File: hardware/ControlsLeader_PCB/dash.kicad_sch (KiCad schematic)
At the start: 11 parts, among them J11 EStop1, J12 EStop2, J13 Supp_In, J14 EStop3, J9 Supp_In

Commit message: Schematic RevA
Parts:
- J11, J12, J13, J14, J9: now fitted
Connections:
- net NMOS Switch/3.3V_LDO renamed NMOS Switch/3.3V_LDO_Switch
- net NMOS Switch1/3.3V_LDO renamed NMOS Switch1/3.3V_LDO_Switch
- net NMOS Switch2/3.3V_LDO renamed NMOS Switch2/3.3V_LDO_Switch
- net NMOS Switch3/3.3V_LDO renamed NMOS Switch3/3.3V_LDO_Switch
- net NMOS Switch4/3.3V_LDO renamed NMOS Switch4/3.3V_LDO_Switch
- net NMOS Switch5/3.3V_LDO renamed NMOS Switch5/3.3V_LDO_Switch
- net NMOS Switch6/3.3V_LDO renamed NMOS Switch6/3.3V_LDO_Switch
- net NMOS Switch8/3.3V_LDO renamed NMOS Switch8/3.3V_LDO_Switch
- net NMOS Switch9/3.3V_LDO renamed NMOS Switch9/3.3V_LDO_Switch
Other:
- sheet NMOS Switch ports: added 3.3V_LDO_Switch; removed 3.3V_LDO
- sheet NMOS Switch1 ports: added 3.3V_LDO_Switch; removed 3.3V_LDO
- sheet NMOS Switch2 ports: added 3.3V_LDO_Switch; removed 3.3V_LDO
- sheet NMOS Switch3 ports: added 3.3V_LDO_Switch; removed 3.3V_LDO
- sheet NMOS Switch4 ports: added 3.3V_LDO_Switch; removed 3.3V_LDO
- sheet NMOS Switch5 ports: added 3.3V_LDO_Switch; removed 3.3V_LDO
- sheet NMOS Switch6 ports: added 3.3V_LDO_Switch; removed 3.3V_LDO
- sheet NMOS Switch8 ports: added 3.3V_LDO_Switch; removed 3.3V_LDO
- sheet NMOS Switch9 ports: added 3.3V_LDO_Switch; removed 3.3V_LDO
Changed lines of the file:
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@@
 	(wire
 		(pts
-			(xy 218.44 54.61) (xy 219.71 54.61)
+			(xy 218.44 50.8) (xy 219.71 50.8)
 		)
 		(stroke
@@
 	(wire
 		(pts
-			(xy 218.44 90.17) (xy 219.71 90.17)
+			(xy 218.44 86.36) (xy 219.71 86.36)
 		)
 		(stroke
@@
 	(wire
 		(pts
-			(xy 120.65 107.95) (xy 121.92 107.95)
+			(xy 120.65 104.14) (xy 121.92 104.14)
 		)
 		(stroke
@@
 	(wire
 		(pts
-			(xy 123.19 86.36) (xy 124.46 86.36)
+			(xy 123.19 82.55) (xy 124.46 82.55)
 		)
 		(stroke
@@
 	(wire
 		(pts
-			(xy 120.65 125.73) (xy 121.92 125.73)
+			(xy 119.38 121.92) (xy 120.65 121.92)
 		)
 		(stroke
@@
 	(wire
 		(pts
-			(xy 123.19 52.07) (xy 124.46 52.07)
+			(xy 123.19 48.26) (xy 124.46 48.26)
 		)
 		(stroke
@@
 	(wire
 		(pts
-			(xy 120.65 142.24) (xy 121.92 142.24)
+			(xy 120.65 138.43) (xy 121.92 138.43)
 		)
 		(stroke
@@
 	(wire
 		(pts
-			(xy 218.44 107.95) (xy 219.71 107.95)
+			(xy 218.44 104.14) (xy 219.71 104.14)
 		)
 		(stroke
@@
 	(wire
 		(pts
-			(xy 123.19 69.85) (xy 124.46 69.85)
+			(xy 123.19 66.04) (xy 124.46 66.04)
 		)
 		(stroke
@@
 	(hierarchical_label "Hazard_GPIO_IN"
 		(shape output)
-		(at 219.71 107.95 0)
+		(at 219.71 104.14 0)
 		(effects
 			(font
@@
 	(hierarchical_label "Cruise_Enable_GPIO_IN"
 		(shape output)
-		(at 219.71 54.61 0)
+		(at 219.71 50.8 0)
 		(effects
 			(font
@@
 	(hierarchical_label "Neuatral_Gear_GPIO"
 		(shape output)
-		(at 124.46 69.85 0)
+		(at 124.46 66.04 0)
 		(effects
 			(font
@@
 	(hierarchical_label "IGN_ARR"
 		(shape output)
-		(at 121.92 125.73 0)
+		(at 120.65 121.92 0)
 		(effects
 			(font
@@
 	(hierarchical_label "REV_SW"
 		(shape output)
-		(at 124.46 86.36 0)
+		(at 124.46 82.55 0)
 		(effects
 			(font
@@
 	(hierarchical_label "Ign_OFF_GPIO"
 		(shape output)
-		(at 121.92 107.95 0)
+		(at 121.92 104.14 0)
 		(effects
 			(font
@@
 	(hierarchical_label "FWD_SW"
 		(shape output)
-		(at 124.46 52.07 0)
+		(at 124.46 48.26 0)
 		(effects
 			(font
@@
 	(hierarchical_label "Regen_Enable_GPIO_IN"
 		(shape output)
-		(at 219.71 90.17 0)
+		(at 219.71 86.36 0)
 		(effects
 			(font
@@
 	(hierarchical_label "IGN_MTR"
 		(shape output)
-		(at 121.92 142.24 0)
+		(at 121.92 138.43 0)
 		(effects
 			(font
@@
 		(exclude_from_sim no)
 		(in_bom yes)
-		(on_board no)
-		(dnp yes)
+		(on_board yes)
+		(dnp no)
 		(property "Reference" "J12"
 			(at 214.63 139.7001 0)
@@
 		(exclude_from_sim no)
 		(in_bom yes)
-		(on_board no)
-		(dnp yes)
+		(on_board yes)
+		(dnp no)
 		(property "Reference" "J11"
 			(at 193.548 136.906 0)
@@
 		(exclude_from_sim no)
 		(in_bom yes)
-		(on_board no)
-		(dnp yes)
+		(on_board yes)
+		(dnp no)
 		(fields_autoplaced yes)
 		(property "Reference" "J9"
@@
 		(exclude_from_sim no)
 		(in_bom yes)
-		(on_board no)
-		(dnp yes)
+		(on_board yes)
+		(dnp no)
 		(fields_autoplaced yes)
 		(property "Reference" "J13"
@@
 		(exclude_from_sim no)
 		(in_bom yes)
-		(on_board no)
-		(dnp yes)
+		(on_board yes)
+		(dnp no)
 		(property "Reference" "J14"
 			(at 232.664 136.906 0)
@@
 		)
 		(pin "GPIO_Signal" output
-			(at 120.65 142.24 0)
+			(at 120.65 138.43 0)
 			(effects
 				(font
@@
 			)
 		)
-		(pin "3.3V_LDO" input
+		(pin "3.3V_LDO_Switch" input
 			(at 93.98 142.24 180)
 			(effects
@@
 		)
 		(pin "GPIO_Signal" output
-			(at 123.19 52.07 0)
+			(at 123.19 48.26 0)
 			(effects
 				(font
@@
 			)
 		)
-		(pin "3.3V_LDO" input
+		(pin "3.3V_LDO_Switch" input
 			(at 96.52 52.07 180)
 			(effects
@@
 		)
 		(pin "GPIO_Signal" output
-			(at 120.65 107.95 0)
+			(at 120.65 104.14 0)
 			(effects
 				(font
@@
 			)
 		)
-		(pin "3.3V_LDO" input
+		(pin "3.3V_LDO_Switch" input
 			(at 93.98 107.95 180)
 			(effects
@@
 		)
 		(pin "GPIO_Signal" output
-			(at 218.44 90.17 0)
+			(at 218.44 86.36 0)
 			(effects
 				(font
@@
 			)
 		)
-		(pin "3.3V_LDO" input
+		(pin "3.3V_LDO_Switch" input
 			(at 191.77 90.17 180)
 			(effects
@@
 		)
 		(pin "GPIO_Signal" output
-			(at 123.19 86.36 0)
+			(at 123.19 82.55 0)
 			(effects
 				(font
@@
 			)
 		)
-		(pin "3.3V_LDO" input
+		(pin "3.3V_LDO_Switch" input
 			(at 96.52 86.36 180)
 			(effects
@@
 		)
 		(pin "GPIO_Signal" output
-			(at 120.65 125.73 0)
+			(at 120.65 121.92 0)
 			(effects
 				(font
@@
 			)
 		)
-		(pin "3.3V_LDO" input
+		(pin "3.3V_LDO_Switch" input
 			(at 93.98 125.73 180)
 			(effects
@@
 		)
 		(pin "GPIO_Signal" output
-			(at 123.19 69.85 0)
+			(at 123.19 66.04 0)
 			(effects
 				(font
@@
 			)
 		)
-		(pin "3.3V_LDO" input
+		(pin "3.3V_LDO_Switch" input
 			(at 96.52 69.85 180)
 			(effects
@@
 		)
 		(pin "GPIO_Signal" output
-			(at 218.44 107.95 0)
+			(at 218.44 104.14 0)
 			(effects
 				(font
@@
 			)
 		)
-		(pin "3.3V_LDO" input
+		(pin "3.3V_LDO_Switch" input
 			(at 191.77 107.95 180)
 			(effects
@@
 		)
 		(pin "GPIO_Signal" output
-			(at 218.44 54.61 0)
+			(at 218.44 50.8 0)
 			(effects
 				(font
@@
 			)
 		)
-		(pin "3.3V_LDO" input
+		(pin "3.3V_LDO_Switch" input
 			(at 191.77 54.61 180)
 			(effects

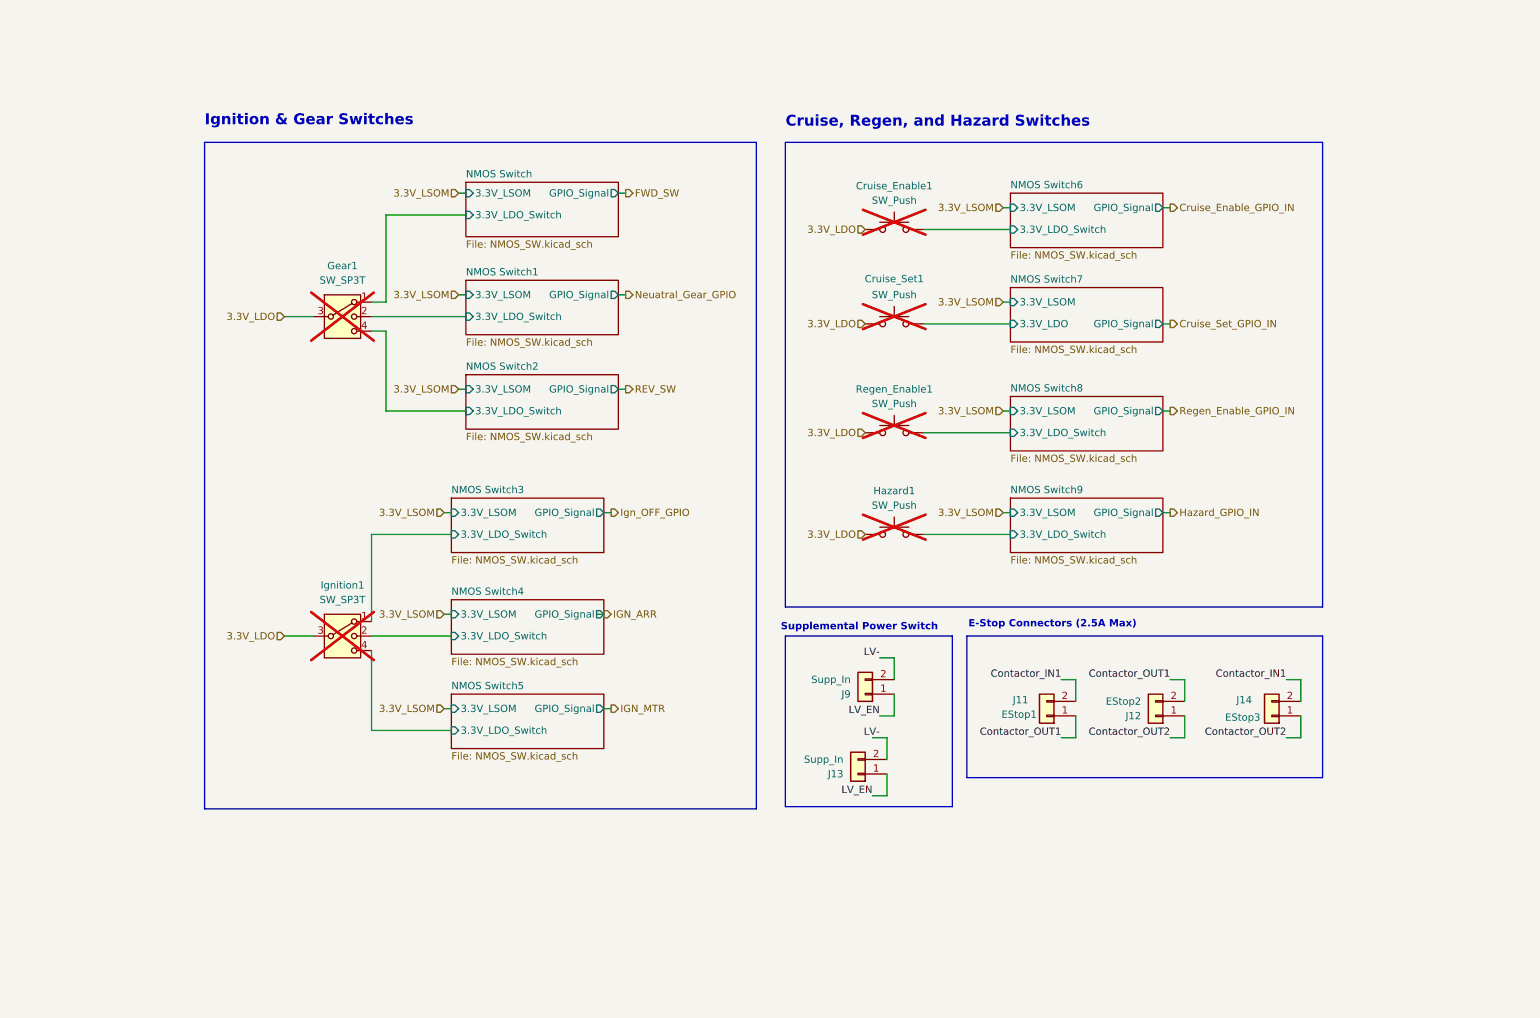
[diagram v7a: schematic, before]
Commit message: PCB DESIGN DONE - need to add datasheets and p/n
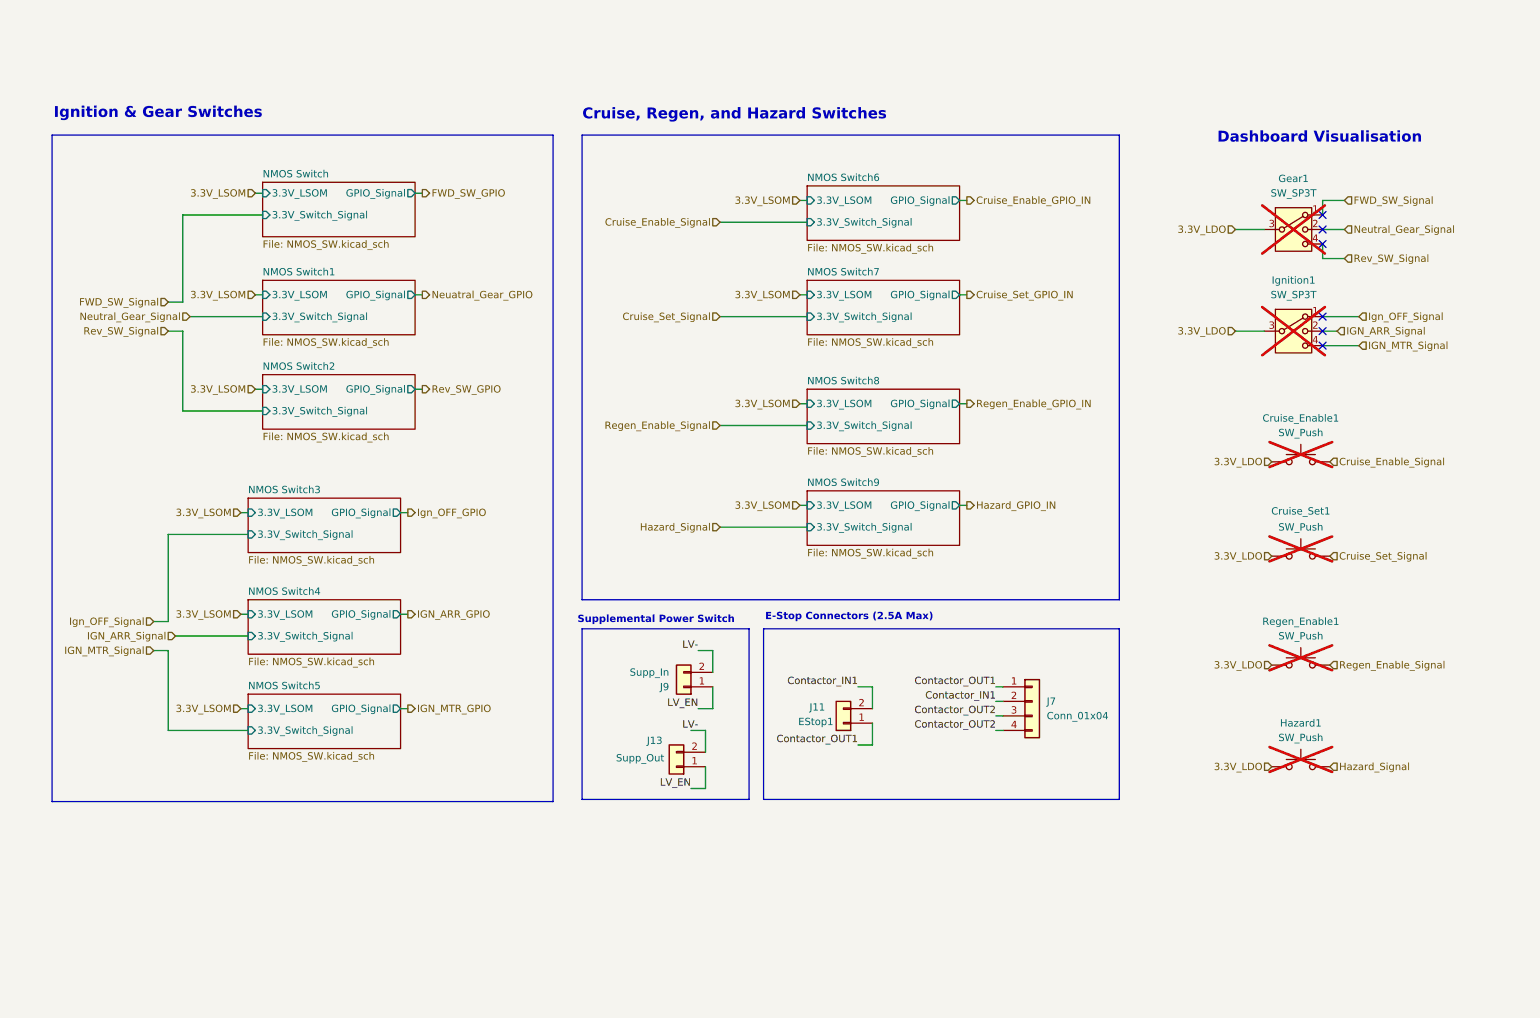
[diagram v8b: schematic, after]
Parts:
- removed J12: EStop2, Connector_Molex:Molex_Micro-Fit_3.0_43650-0215_1x02_P3.00mm_Vertical, symbol Connector_Generic:Conn_01x02
- removed J14: EStop3, Connector_Molex:Molex_Micro-Fit_3.0_43650-0215_1x02_P3.00mm_Vertical, symbol Connector_Generic:Conn_01x02
- added J7: Conn_01x04, Connector_Molex:Molex_Nano-Fit_105313-xx04_1x04_P2.50mm_Horizontal, symbol Connector_Generic:Conn_01x04
- J11, J9: footprint Connector_Molex:Molex_Micro-Fit_3.0_43650-0215_1x02_P3.00mm_Vertical -> Connector_Molex:Molex_Nano-Fit_105313-xx02_1x02_P2.50mm_Horizontal
- J13: value Supp_In -> Supp_Out; footprint Connector_Molex:Molex_Micro-Fit_3.0_43650-0215_1x02_P3.00mm_Vertical -> Connector_Molex:Molex_Nano-Fit_105313-xx02_1x02_P2.50mm_Horizontal
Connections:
- net Contactor_IN1: now also J7.2 (Pin_2)
- net Contactor_OUT1: now also J7.1 (Pin_1)
- net Contactor_OUT2: now also J7.3 (Pin_3), J7.4 (Pin_4)
- net NMOS Switch/3.3V_LDO_Switch renamed FWD_SW_Signal
- net NMOS Switch1/3.3V_LDO_Switch renamed Neutral_Gear_Signal
- net NMOS Switch2/3.3V_LDO_Switch renamed Rev_SW_Signal
- net NMOS Switch3/3.3V_LDO_Switch renamed Ign_OFF_Signal
- net NMOS Switch4/3.3V_LDO_Switch renamed IGN_ARR_Signal
- net NMOS Switch5/3.3V_LDO_Switch renamed IGN_MTR_Signal
- net NMOS Switch6/3.3V_LDO_Switch renamed Cruise_Enable_Signal
- net NMOS Switch7/3.3V_LDO renamed Cruise_Set_Signal
- net NMOS Switch8/3.3V_LDO_Switch renamed Regen_Enable_Signal
- net NMOS Switch9/3.3V_LDO_Switch renamed Hazard_Signal
- no-connect marks 0 -> 6
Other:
- sheet NMOS Switch ports: added 3.3V_Switch_Signal; removed 3.3V_LDO_Switch
- sheet NMOS Switch1 ports: added 3.3V_Switch_Signal; removed 3.3V_LDO_Switch
- sheet NMOS Switch2 ports: added 3.3V_Switch_Signal; removed 3.3V_LDO_Switch
- sheet NMOS Switch3 ports: added 3.3V_Switch_Signal; removed 3.3V_LDO_Switch
- sheet NMOS Switch4 ports: added 3.3V_Switch_Signal; removed 3.3V_LDO_Switch
- sheet NMOS Switch5 ports: added 3.3V_Switch_Signal; removed 3.3V_LDO_Switch
- sheet NMOS Switch6 ports: added 3.3V_Switch_Signal; removed 3.3V_LDO_Switch
- sheet NMOS Switch7 ports: added 3.3V_Switch_Signal; removed 3.3V_LDO
- sheet NMOS Switch8 ports: added 3.3V_Switch_Signal; removed 3.3V_LDO_Switch
- sheet NMOS Switch9 ports: added 3.3V_Switch_Signal; removed 3.3V_LDO_Switch
- note added: "Dashboard Visualisation"
- moved on the sheet: Cruise_Enable1, Cruise_Set1, Gear1, Hazard1, Ignition1, J11, J13, J9, Regen_Enable1
